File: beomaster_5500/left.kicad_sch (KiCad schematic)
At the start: 74 parts, among them Q201 BF423, Q202 BF857, Q203 BDV65B, Q204 BC547B, Q205 BF422, Q206 BC547B, Q207 BC547B, Q208 BC557B, Q209 BDV64B, Q210 BC547B, Q211 BF857, Q212 MPSA13, Q213 BC547B

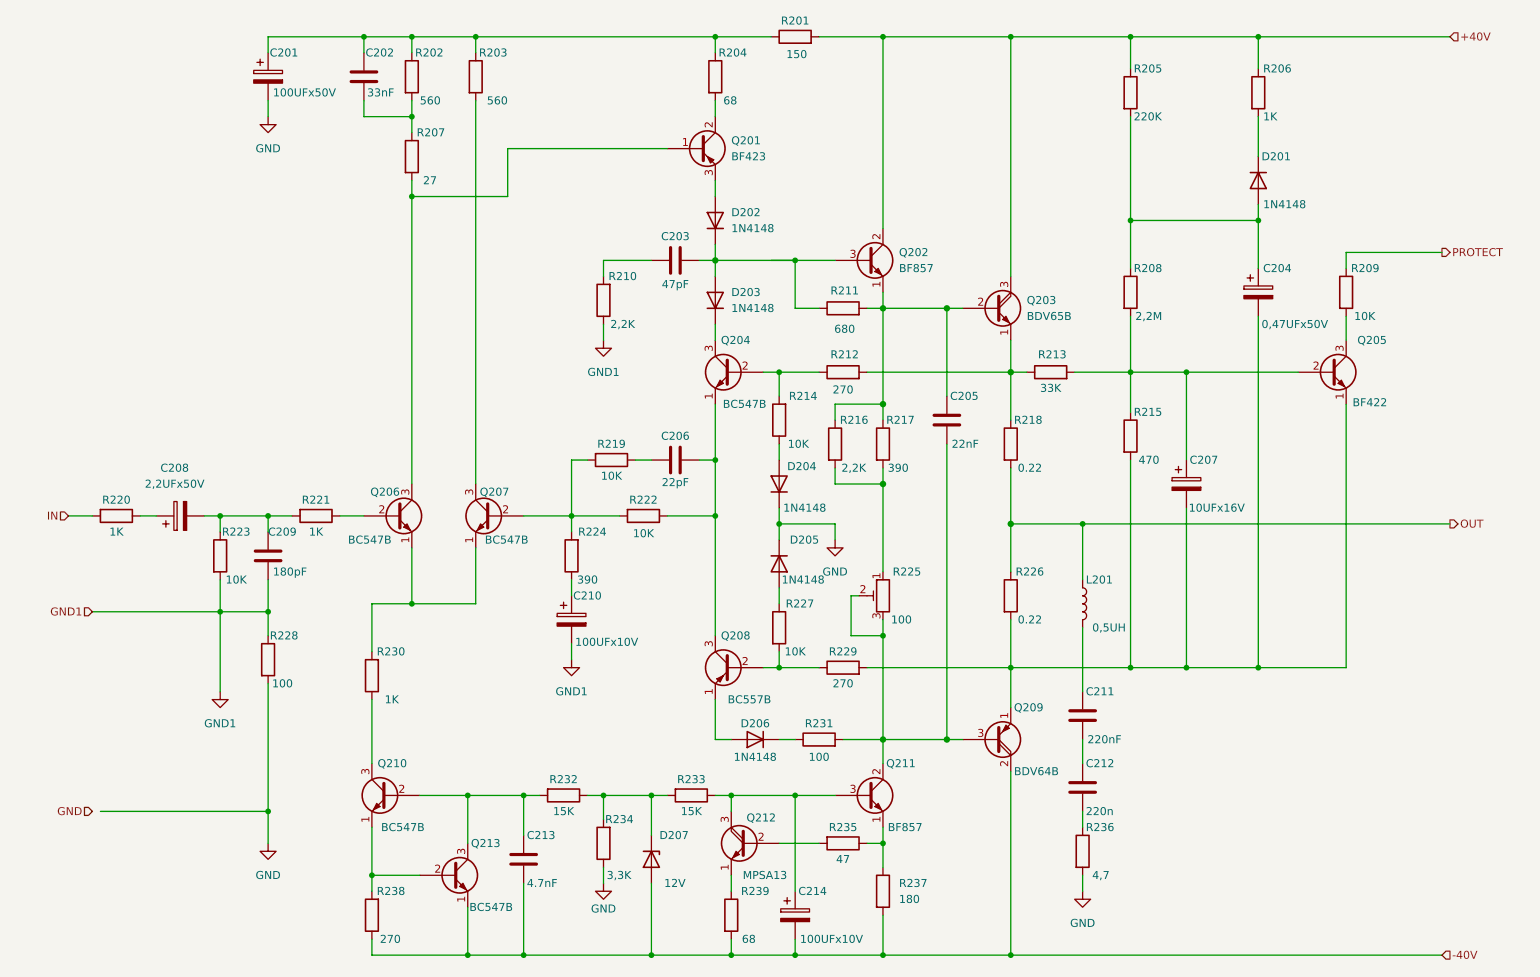
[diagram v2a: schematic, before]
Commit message: add capacitor foot print
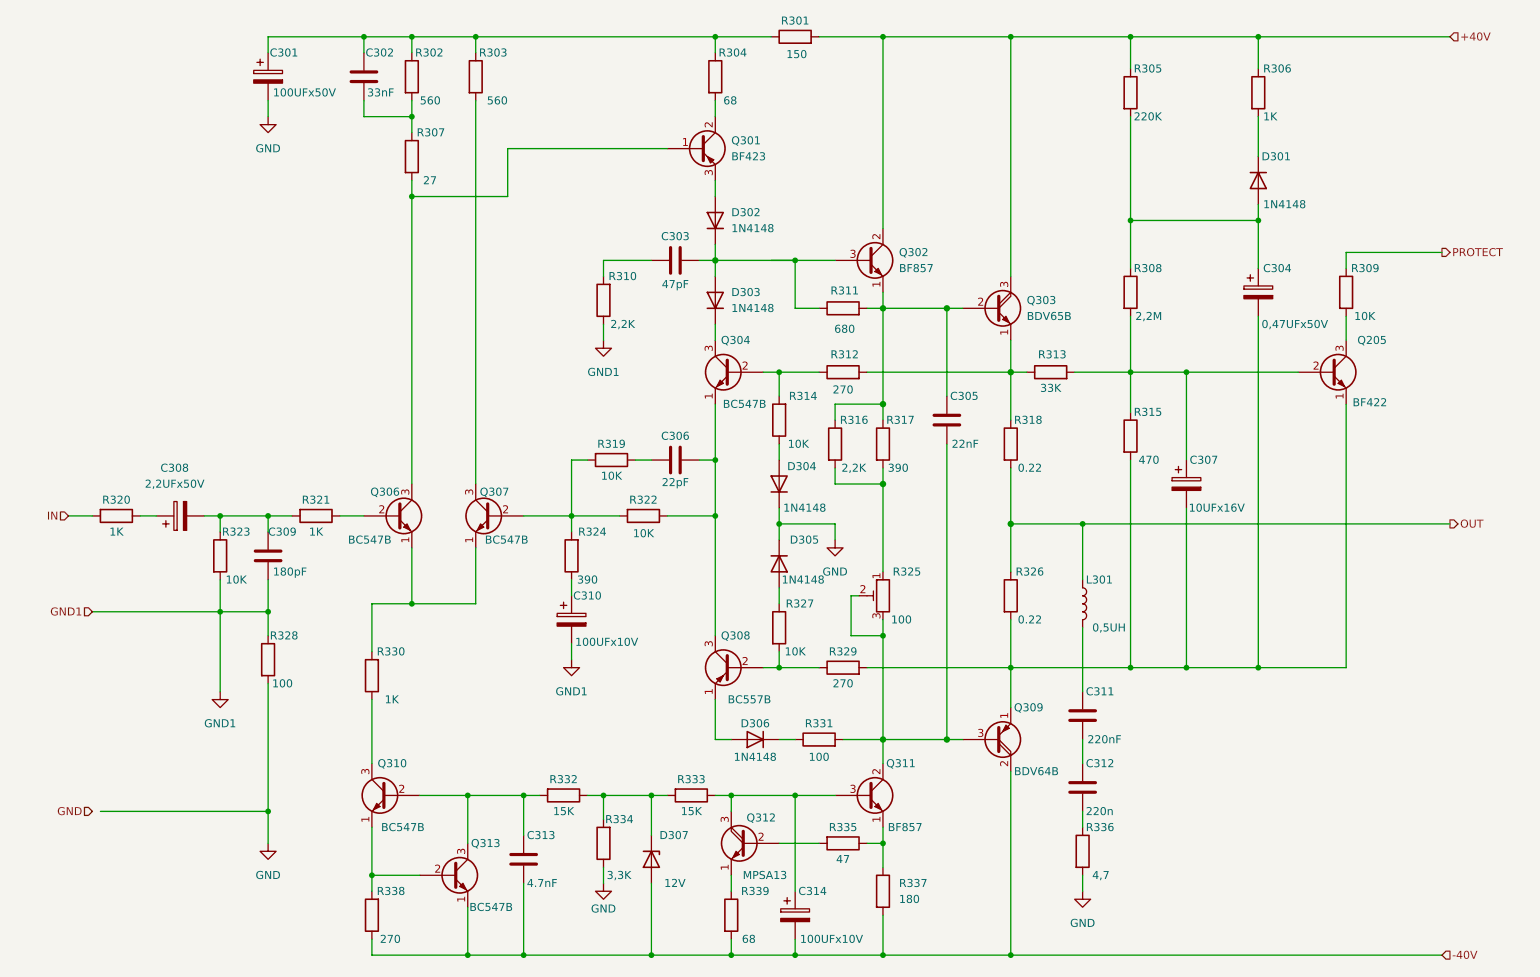
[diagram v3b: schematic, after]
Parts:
- removed C201: 100UFx50V, symbol Device:C_Polarized
- removed C202: 33nF, symbol Device:C
- removed C203: 47pF, symbol Device:C
- removed C204: 0,47UFx50V, symbol Device:C_Polarized
- removed C205: 22nF, symbol Device:C
- removed C206: 22pF, symbol Device:C
- removed C207: 10UFx16V, symbol Device:C_Polarized
- removed C208: 2,2UFx50V, symbol Device:C_Polarized
- removed C209: 180pF, symbol Device:C
- removed C210, C214: 100UFx10V, symbol Device:C_Polarized
- removed C211: 220nF, symbol Device:C
- removed C212: 220n, symbol Device:C
- removed C213: 4.7nF, symbol Device:C
- removed D201, D202, D203, D204, D205, D206: 1N4148, Diode_THT:D_DO-35_SOD27_P10.16mm_Horizontal, symbol Device:D
- removed D207: 12V, Diode_THT:D_DO-35_SOD27_P10.16mm_Horizontal, symbol Device:D_Zener
- removed L201: 0,5UH, Inductor_THT:L_Radial_L10.2mm_W10.2mm_Px7.62mm_Py7.62mm_Pulse_LP-30, symbol Device:L
- removed Q201: BF423, Package_TO_SOT_THT:TO-92_Inline_Wide, symbol Device:Q_PNP_BCE
- removed Q202, Q211: BF857, Package_TO_SOT_THT:TO-220-3_Vertical, symbol Device:Q_NPN_ECB
- removed Q203: BDV65B, Package_TO_SOT_THT:TO-247-3_Vertical, symbol Device:Q_NPN_Darlington_EBC
- removed Q204, Q206, Q207, Q210, Q213: BC547B, Package_TO_SOT_THT:TO-92_Inline_Wide, symbol Device:Q_NPN_EBC
- removed Q208: BC557B, Package_TO_SOT_THT:TO-92_Inline_Wide, symbol Device:Q_PNP_EBC
- removed Q209: BDV64B, Package_TO_SOT_THT:TO-247-3_Vertical, symbol Device:Q_PNP_Darlington_ECB
- removed Q212: MPSA13, Package_TO_SOT_THT:TO-92_Inline_Wide, symbol Device:Q_NPN_Darlington_EBC
- removed R201: 150, Resistor_THT:R_Axial_DIN0207_L6.3mm_D2.5mm_P10.16mm_Horizontal, symbol Device:R
- removed R202, R203: 560, Resistor_THT:R_Axial_DIN0207_L6.3mm_D2.5mm_P10.16mm_Horizontal, symbol Device:R
- removed R204, R239: 68, Resistor_THT:R_Axial_DIN0207_L6.3mm_D2.5mm_P10.16mm_Horizontal, symbol Device:R
- removed R205: 220K, Resistor_THT:R_Axial_DIN0207_L6.3mm_D2.5mm_P10.16mm_Horizontal, symbol Device:R
- removed R206, R220, R221, R230: 1K, Resistor_THT:R_Axial_DIN0207_L6.3mm_D2.5mm_P10.16mm_Horizontal, symbol Device:R
- removed R207: 27, Resistor_THT:R_Axial_DIN0207_L6.3mm_D2.5mm_P10.16mm_Horizontal, symbol Device:R
- removed R208: 2,2M, Resistor_THT:R_Axial_DIN0207_L6.3mm_D2.5mm_P10.16mm_Horizontal, symbol Device:R
- removed R209, R214, R219, R222, R223, R227: 10K, Resistor_THT:R_Axial_DIN0207_L6.3mm_D2.5mm_P10.16mm_Horizontal, symbol Device:R
- removed R210, R216: 2,2K, Resistor_THT:R_Axial_DIN0207_L6.3mm_D2.5mm_P10.16mm_Horizontal, symbol Device:R
- removed R211: 680, Resistor_THT:R_Axial_DIN0207_L6.3mm_D2.5mm_P10.16mm_Horizontal, symbol Device:R
- removed R212, R229, R238: 270, Resistor_THT:R_Axial_DIN0207_L6.3mm_D2.5mm_P10.16mm_Horizontal, symbol Device:R
- removed R213: 33K, Resistor_THT:R_Axial_DIN0207_L6.3mm_D2.5mm_P10.16mm_Horizontal, symbol Device:R
- removed R215: 470, Resistor_THT:R_Axial_DIN0207_L6.3mm_D2.5mm_P10.16mm_Horizontal, symbol Device:R
- removed R217, R224: 390, Resistor_THT:R_Axial_DIN0207_L6.3mm_D2.5mm_P10.16mm_Horizontal, symbol Device:R
- removed R218, R226: 0.22, Resistor_THT:R_Axial_DIN0207_L6.3mm_D2.5mm_P10.16mm_Horizontal, symbol Device:R
- removed R225: 100, Potentiometer_THT:Potentiometer_Bourns_3296Y_Vertical, symbol Device:R_Potentiometer_Trim
- removed R228, R231: 100, Resistor_THT:R_Axial_DIN0207_L6.3mm_D2.5mm_P10.16mm_Horizontal, symbol Device:R
- removed R232, R233: 15K, Resistor_THT:R_Axial_DIN0207_L6.3mm_D2.5mm_P10.16mm_Horizontal, symbol Device:R
- removed R234: 3,3K, Resistor_THT:R_Axial_DIN0207_L6.3mm_D2.5mm_P10.16mm_Horizontal, symbol Device:R
- removed R235: 47, Resistor_THT:R_Axial_DIN0207_L6.3mm_D2.5mm_P10.16mm_Horizontal, symbol Device:R
- removed R236: 4,7, Resistor_THT:R_Axial_DIN0207_L6.3mm_D2.5mm_P10.16mm_Horizontal, symbol Device:R
- removed R237: 180, Resistor_THT:R_Axial_DIN0207_L6.3mm_D2.5mm_P10.16mm_Horizontal, symbol Device:R
- added C301: 100UFx50V, Capacitor_THT:CP_Radial_D10.0mm_P7.50mm, symbol Device:C_Polarized
- added C302: 33nF, symbol Device:C
- added C303: 47pF, symbol Device:C
- added C304: 0,47UFx50V, symbol Device:C_Polarized
- added C305: 22nF, symbol Device:C
- added C306: 22pF, symbol Device:C
- added C307: 10UFx16V, Capacitor_THT:CP_Radial_D8.0mm_P5.00mm, symbol Device:C_Polarized
- added C308: 2,2UFx50V, symbol Device:C_Polarized
- added C309: 180pF, symbol Device:C
- added C310: 100UFx10V, symbol Device:C_Polarized
- added C311: 220nF, symbol Device:C
- added C312: 220n, symbol Device:C
- added C313: 4.7nF, symbol Device:C
- added C314: 100UFx10V, Capacitor_THT:CP_Radial_D8.0mm_P5.00mm, symbol Device:C_Polarized
- added D301, D302, D303, D304, D305, D306: 1N4148, Diode_THT:D_DO-35_SOD27_P10.16mm_Horizontal, symbol Device:D
- added D307: 12V, Diode_THT:D_DO-35_SOD27_P10.16mm_Horizontal, symbol Device:D_Zener
- added L301: 0,5UH, Inductor_THT:L_Radial_L10.2mm_W10.2mm_Px7.62mm_Py7.62mm_Pulse_LP-30, symbol Device:L
- added Q301: BF423, Package_TO_SOT_THT:TO-92_Inline_Wide, symbol Device:Q_PNP_BCE
- added Q302, Q311: BF857, Package_TO_SOT_THT:TO-220-3_Vertical, symbol Device:Q_NPN_ECB
- added Q303: BDV65B, Package_TO_SOT_THT:TO-247-3_Vertical, symbol Device:Q_NPN_Darlington_EBC
- added Q304, Q306, Q307, Q310, Q313: BC547B, Package_TO_SOT_THT:TO-92_Inline_Wide, symbol Device:Q_NPN_EBC
- added Q308: BC557B, Package_TO_SOT_THT:TO-92_Inline_Wide, symbol Device:Q_PNP_EBC
- added Q309: BDV64B, Package_TO_SOT_THT:TO-247-3_Vertical, symbol Device:Q_PNP_Darlington_ECB
- added Q312: MPSA13, Package_TO_SOT_THT:TO-92_Inline_Wide, symbol Device:Q_NPN_Darlington_EBC
- added R301: 150, Resistor_THT:R_Axial_DIN0207_L6.3mm_D2.5mm_P10.16mm_Horizontal, symbol Device:R
- added R302, R303: 560, Resistor_THT:R_Axial_DIN0207_L6.3mm_D2.5mm_P10.16mm_Horizontal, symbol Device:R
- added R304, R339: 68, Resistor_THT:R_Axial_DIN0207_L6.3mm_D2.5mm_P10.16mm_Horizontal, symbol Device:R
- added R305: 220K, Resistor_THT:R_Axial_DIN0207_L6.3mm_D2.5mm_P10.16mm_Horizontal, symbol Device:R
- added R306, R320, R321, R330: 1K, Resistor_THT:R_Axial_DIN0207_L6.3mm_D2.5mm_P10.16mm_Horizontal, symbol Device:R
- added R307: 27, Resistor_THT:R_Axial_DIN0207_L6.3mm_D2.5mm_P10.16mm_Horizontal, symbol Device:R
- added R308: 2,2M, Resistor_THT:R_Axial_DIN0207_L6.3mm_D2.5mm_P10.16mm_Horizontal, symbol Device:R
- added R309, R314, R319, R322, R323, R327: 10K, Resistor_THT:R_Axial_DIN0207_L6.3mm_D2.5mm_P10.16mm_Horizontal, symbol Device:R
- added R310, R316: 2,2K, Resistor_THT:R_Axial_DIN0207_L6.3mm_D2.5mm_P10.16mm_Horizontal, symbol Device:R
- added R311: 680, Resistor_THT:R_Axial_DIN0207_L6.3mm_D2.5mm_P10.16mm_Horizontal, symbol Device:R
- added R312, R329, R338: 270, Resistor_THT:R_Axial_DIN0207_L6.3mm_D2.5mm_P10.16mm_Horizontal, symbol Device:R
- added R313: 33K, Resistor_THT:R_Axial_DIN0207_L6.3mm_D2.5mm_P10.16mm_Horizontal, symbol Device:R
- added R315: 470, Resistor_THT:R_Axial_DIN0207_L6.3mm_D2.5mm_P10.16mm_Horizontal, symbol Device:R
- added R317, R324: 390, Resistor_THT:R_Axial_DIN0207_L6.3mm_D2.5mm_P10.16mm_Horizontal, symbol Device:R
- added R318, R326: 0.22, Resistor_THT:R_Axial_DIN0207_L6.3mm_D2.5mm_P10.16mm_Horizontal, symbol Device:R
- added R325: 100, Potentiometer_THT:Potentiometer_Bourns_3296Y_Vertical, symbol Device:R_Potentiometer_Trim
- added R328, R331: 100, Resistor_THT:R_Axial_DIN0207_L6.3mm_D2.5mm_P10.16mm_Horizontal, symbol Device:R
- added R332, R333: 15K, Resistor_THT:R_Axial_DIN0207_L6.3mm_D2.5mm_P10.16mm_Horizontal, symbol Device:R
- added R334: 3,3K, Resistor_THT:R_Axial_DIN0207_L6.3mm_D2.5mm_P10.16mm_Horizontal, symbol Device:R
- added R335: 47, Resistor_THT:R_Axial_DIN0207_L6.3mm_D2.5mm_P10.16mm_Horizontal, symbol Device:R
- added R336: 4,7, Resistor_THT:R_Axial_DIN0207_L6.3mm_D2.5mm_P10.16mm_Horizontal, symbol Device:R
- added R337: 180, Resistor_THT:R_Axial_DIN0207_L6.3mm_D2.5mm_P10.16mm_Horizontal, symbol Device:R
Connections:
- net +40V: now also Q302.2 (C), Q303.3 (C), R301.2, R305.1, R306.1
- net -40V: now also C313.2, C314.2, D307.2 (A), Q309.2 (C), Q313.1 (E), R337.2, R338.1, R339.2
- net GND: now also C301.2, D304.1 (K), D305.1 (K), R328.2, R334.1, R336.2
- net GND1: now also C309.2, C310.2, R310.1, R323.2, R328.1
- net IN: now also R320.2
- net OUT: now also L301.1, R318.2, R326.1
- net PROTECT: now also R309.1
- net at Q205.3 (C): now also R309.2
- net at Q205.1 (E): now also C304.2, C307.2, Q309.1 (E), R315.2, R326.2, R329.2
- net at Q205.2 (B): now also C307.1, R308.2, R313.2, R315.1
- new net: D301.1 (K), R306.2
- new net: C313.1, Q310.2 (B), Q313.3 (C), R332.2
- new net: C302.2, R302.2, R307.1
- new net: Q301.1 (B), Q306.3 (C), R307.2
- new net: C303.2, D302.1 (K), D303.2 (A), Q302.3 (B), R311.1
- new net: C305.1, Q302.1 (E), Q303.2 (B), R311.2, R316.1, R317.1
- new net: Q310.1 (E), Q313.2 (B), R338.2
- new net: Q306.2 (B), R321.1
- new net: C308.2, C309.1, R321.2, R323.1
- new net: C311.2, C312.1
- new net: C312.2, R336.1
- new net: D307.1 (K), R332.1, R333.2, R334.2
- new net: C304.1, D301.2 (A), R305.2, R308.1
- new net: Q301.2 (C), R304.2
- new net: D302.2 (A), Q301.3 (E)
- new net: C314.1, Q311.3 (B), Q312.3 (C), R333.1
- new net: C301.1, C302.1, R301.1, R302.1, R303.1, R304.1
- new net: C310.1, R324.1
- new net: Q307.2 (B), R319.2, R322.2, R324.2
- new net: C305.2, Q309.3 (B), Q311.2 (C), R325.2, R325.3, R331.2
- new net: C308.1, R320.1
- new net: Q306.1 (E), Q307.1 (E), R330.2
- new net: C311.1, L301.2
- new net: Q304.2 (B), R312.1, R314.2
- new net: Q303.1 (E), R312.2, R313.1, R318.1
- new net: C306.2, Q304.1 (E), Q308.3 (C), R322.1
- new net: D303.1 (K), Q304.3 (C)
- new net: D304.2 (A), R314.1
- new net: C306.1, R319.1
- new net: Q308.2 (B), R327.2, R329.1
- new net: D306.1 (K), R331.1
- new net: D306.2 (A), Q308.1 (E)
- new net: C303.1, R310.2
- new net: Q310.3 (C), R330.1
- new net: Q312.1 (E), R339.1
- new net: Q312.2 (B), R335.2
- new net: D305.2 (A), R327.1
- new net: Q307.3 (C), R303.2
- new net: Q311.1 (E), R335.1, R337.1
- new net: R316.2, R317.2, R325.1

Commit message: improve schema
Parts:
- renumbered C301 to C201, C302 to C202, C303 to C203, C304 to C204, C305 to C205, C306 to C206, C307 to C207, C308 to C208, C309 to C209, C310 to C210, C311 to C211, C312 to C212, C313 to C213, C314 to C214, D301 to D201, D302 to D202, D303 to D203, D304 to D204, D305 to D205, D306 to D206, D307 to D207, L301 to L201, Q301 to Q201, Q302 to Q202, Q303 to Q203, Q304 to Q204, Q306 to Q206, Q307 to Q207, Q308 to Q208, Q309 to Q209, Q310 to Q210, Q311 to Q211, Q312 to Q212, Q313 to Q213, R301 to R201, R302 to R202, R303 to R203, R304 to R204, R305 to R205, R306 to R206, R307 to R207, R308 to R208, R309 to R209, R310 to R210, R311 to R211, R312 to R212, R313 to R213, R314 to R214, R315 to R215, R316 to R216, R317 to R217, R318 to R218, R319 to R219, R320 to R220, R321 to R221, R322 to R222, R323 to R223, R324 to R224, R325 to R225, R326 to R226, R327 to R227, R328 to R228, R329 to R229, R330 to R230, R331 to R231, R332 to R232, R333 to R233, R334 to R234, R335 to R235, R336 to R236, R337 to R237, R338 to R238, R339 to R239
